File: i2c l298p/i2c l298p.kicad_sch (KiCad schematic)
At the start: 119 parts, among them J1 power in, J2 Conn_01x04, J4 Conn_01x04, J6 to qwiic breakout, J7 qwiic 1, J8 qwiic 2, U1 ILQ620GB-X009, U2 ILQ620GB-X009, U3 ILQ620GB-X009, U5 PCA9685PW

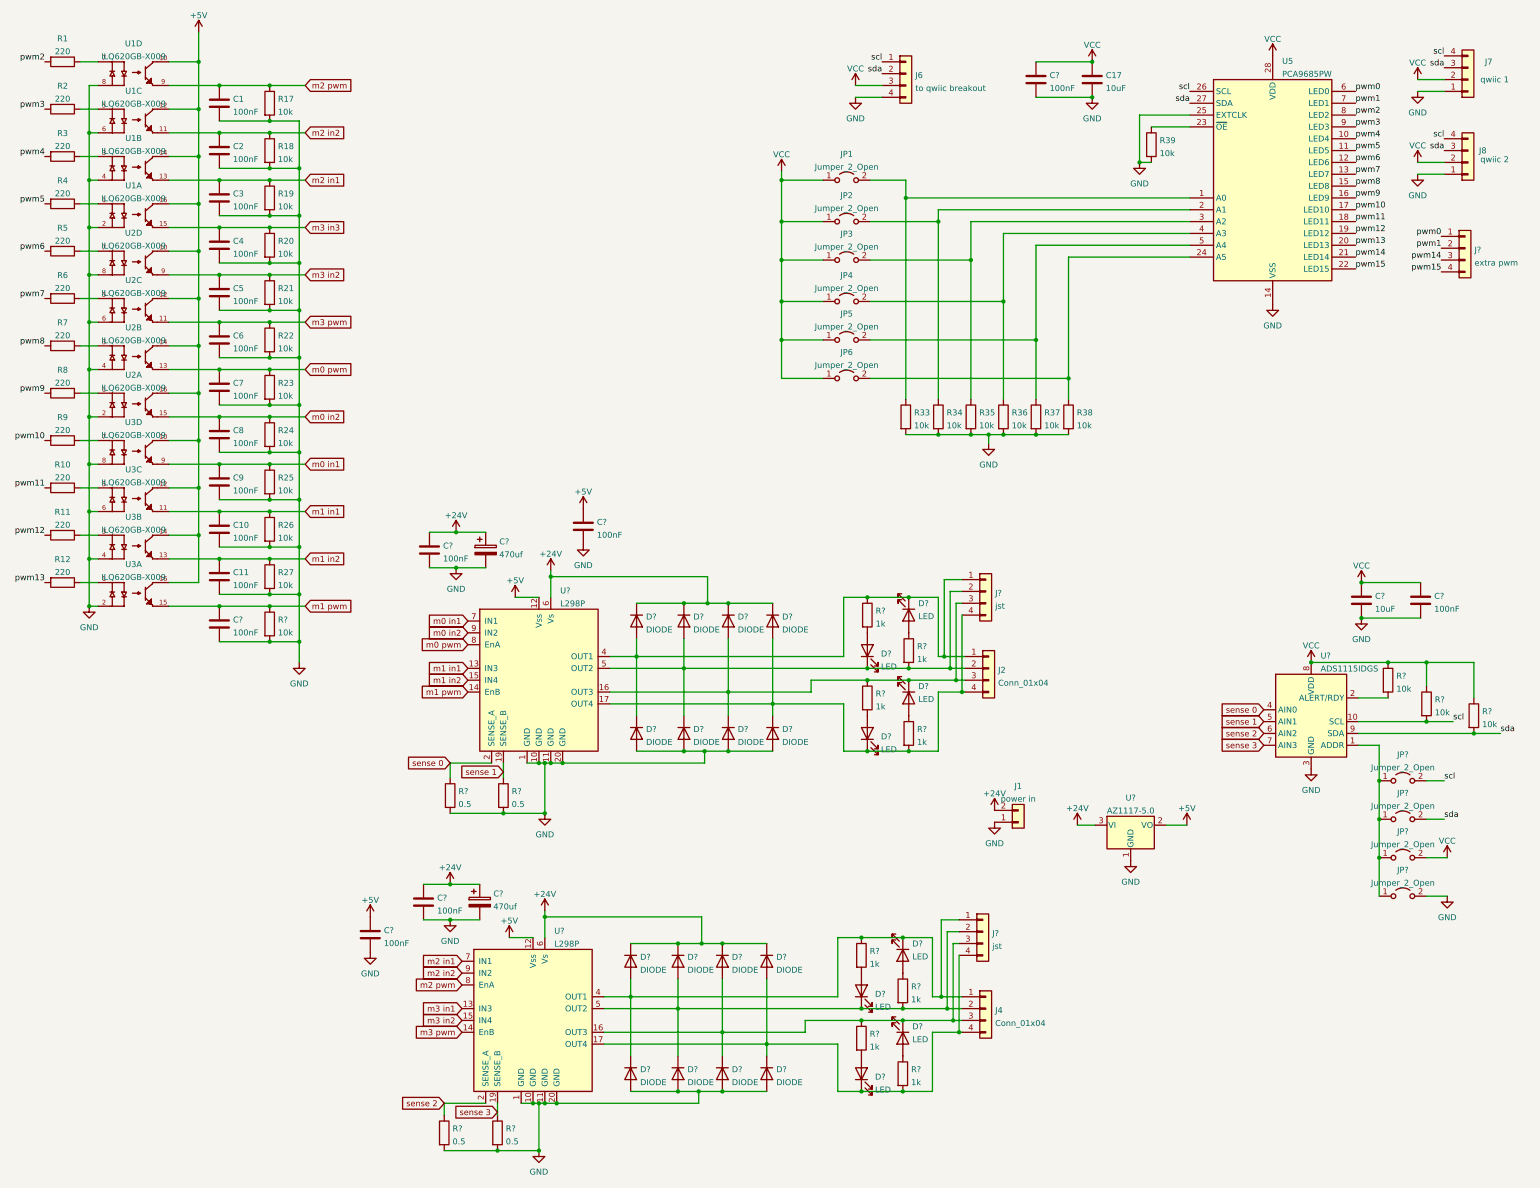
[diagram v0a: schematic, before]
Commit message: finished motor controller layout
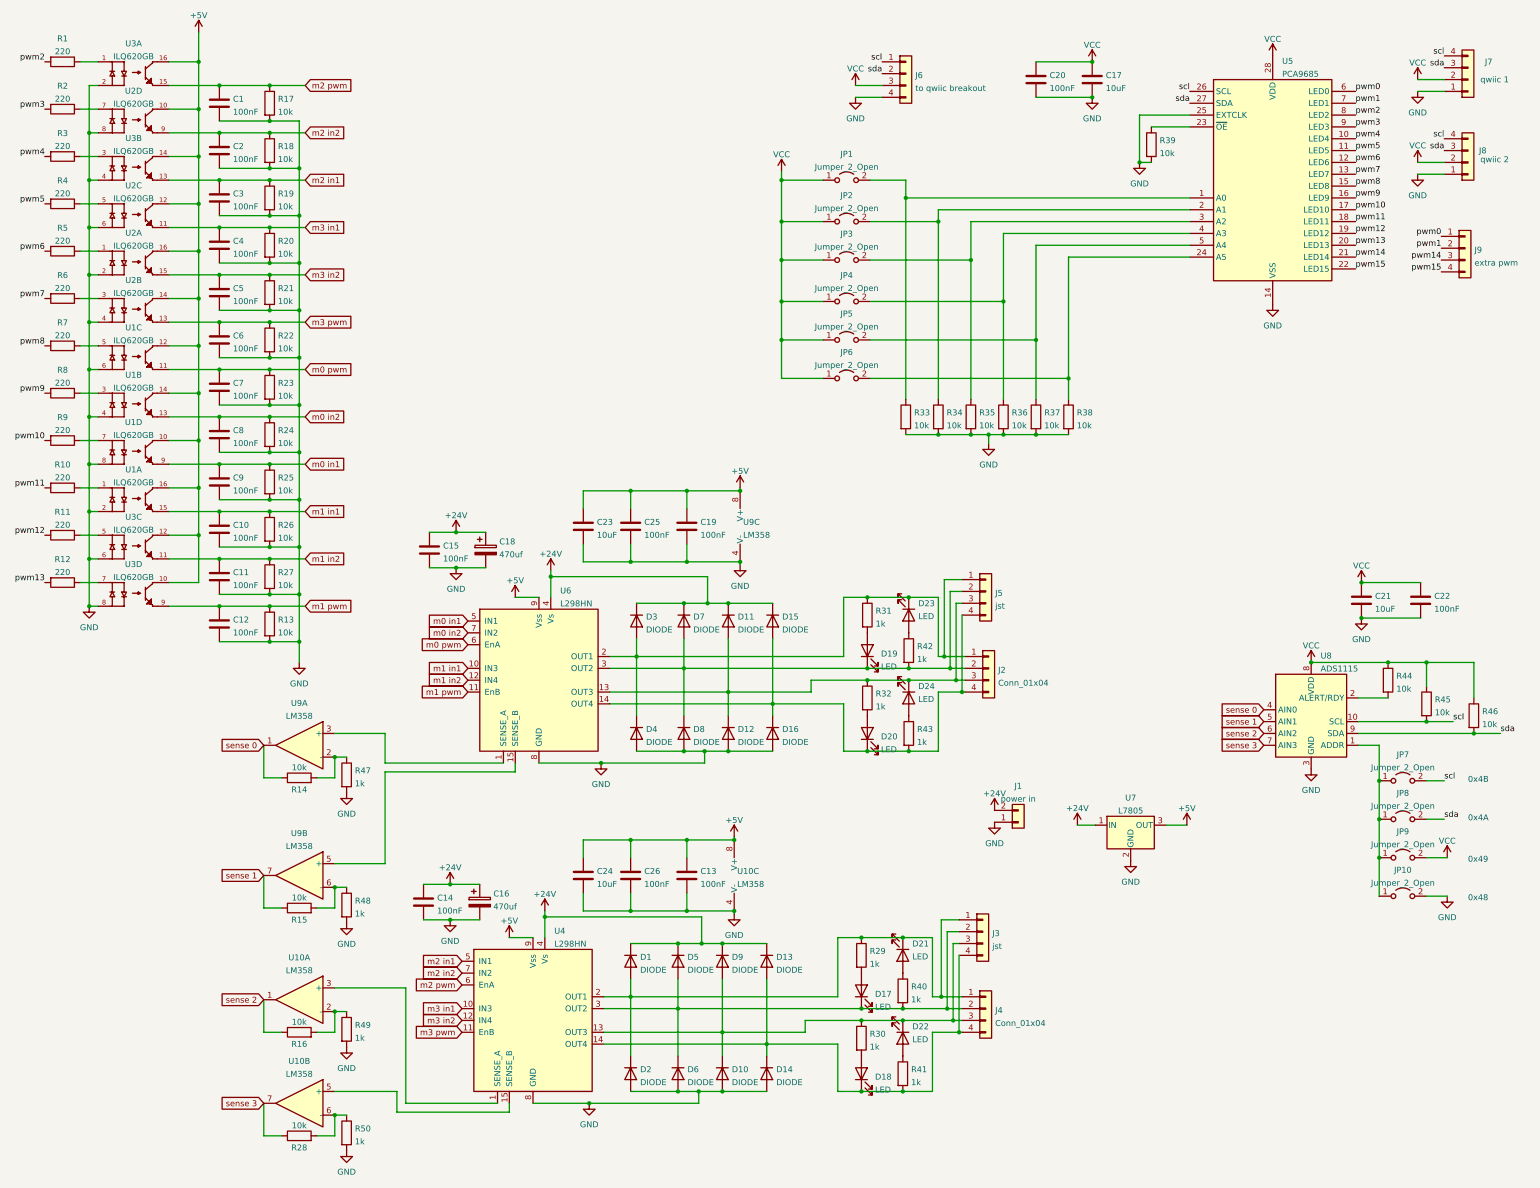
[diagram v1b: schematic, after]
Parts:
- removed R? (x4): 0.5, symbol Device:R
- removed U? (x2): L298P, symbol Driver_Motor:L298P
- removed U?: AZ1117-5.0, symbol Regulator_Linear:AZ1117-5.0
- added C23, C24: 10uF, Capacitor_SMD:C_0603_1608Metric, symbol Device:C
- added C25, C26: 100nF, Capacitor_SMD:C_0603_1608Metric, symbol Device:C
- added R14, R15, R16, R28: 10k, Resistor_SMD:R_0603_1608Metric, symbol Device:R
- added R47, R48, R49, R50: 1k, Resistor_SMD:R_0603_1608Metric, symbol Device:R
- added U10, U9: LM358, Package_SO:SOIC-8_3.9x4.9mm_P1.27mm, symbol Amplifier_Operational:LM358
- added U4, U6: L298HN, Package_TO_SOT_THT:TO-220-15_P2.54x2.54mm_StaggerOdd_Lead4.58mm_Vertical, symbol Driver_Motor:L298HN
- added U7: L7805, Package_TO_SOT_THT:TO-220-3_Horizontal_TabDown, symbol Regulator_Linear:L7805
- C16, C18: renamed from C?; footprint (none) -> Capacitor_THT:CP_Radial_D8.0mm_P3.50mm
- D1, D10, D11, D12, D13, D14, D15, D16, D2, D3, D4, D5, D6, D7, D8, D9: renamed from D?; footprint (none) -> Diode_SMD:D_SMA
- D17, D18, D19, D20, D21, D22, D23, D24: renamed from D?; footprint (none) -> LED_SMD:LED_0603_1608Metric
- J3, J5: renamed from J?; footprint TerminalBlock_Phoenix:TerminalBlock_Phoenix_MKDS-1,5-4_1x04_P5.00mm_Horizontal -> Connector_JST:JST_XH_B4B-XH-A_1x04_P2.50mm_Vertical
- J9: renamed from J?; footprint (none) -> Connector_PinHeader_2.54mm:PinHeader_1x04_P2.54mm_Vertical
- R29, R30, R31, R32, R40, R41, R42, R43: renamed from R?; footprint (none) -> Resistor_SMD:R_0603_1608Metric
- U1, U2, U3: value ILQ620GB-X009 -> ILQ620GB
- U5: value PCA9685PW -> PCA9685
- U8: renamed from U?; value ADS1115IDGS -> ADS1115
- gave numbers to parts that had none: 16
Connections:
- net +24V: now also U4.4 (Vs), U6.4 (Vs), U7.1 (IN)
- net +5V: now also C23.1, C24.1, C25.1, C26.1, U10.8 (V+), U4.9 (Vss), U6.9 (Vss), U7.3 (OUT), U9.8 (V+)
- net GND: now also C23.2, C24.2, C25.2, C26.2, R47.2, R48.2, R49.2, R50.2, U10.4 (V-), U4.8 (GND), U6.8 (GND), U7.2 (GND), U9.4 (V-)
- net m0 in1: now also U1.9, U6.5 (IN1); no longer U3.9
- net m0 in2: now also U1.13, U6.7 (IN2); no longer U2.15
- net m0 pwm: now also U1.11, U6.6 (EnA); no longer U2.13
- net m1 in1: now also U1.15, U6.10 (IN3); no longer U3.11
- net m1 in2: now also U3.11, U6.12 (IN4); no longer U3.13
- net m1 pwm: now also U3.9, U6.11 (EnB); no longer U3.15
- net m2 in1: now also U3.13, U4.5 (IN1); no longer U1.13
- net m2 in2: now also U2.9, U4.7 (IN2); no longer U1.11
- net m2 pwm: now also U3.15, U4.6 (EnA); no longer U1.9
- net m3 in1: now also C4.1, R20.1, U2.11, U4.10 (IN3)
- net m3 in2: now also U2.15, U4.12 (IN4); no longer U2.9
- net m3 pwm: now also U2.13, U4.11 (EnB); no longer U2.11
- net sense 0: now also R14.1, U9.1
- net sense 1: now also R15.1, U9.7
- net sense 2: now also R16.1, U10.1
- net sense 3: now also R28.1, U10.7
- net at D23.1 (K), D3.1 (A), D4.2 (K)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: now also U6.2 (OUT1)
- net at R6.1: now also U2.3; no longer U2.5
- net at D17.1 (K), D5.1 (A), D6.2 (K)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: now also U4.3 (OUT2)
- net at U1.3: now also R8.1; no longer R3.1
- net at U2.1: now also R5.1; no longer R8.1
- net at D15.1 (A), D16.2 (K), D20.1 (K)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: now also U6.14 (OUT4)
- net at R7.1: now also U1.5; no longer U2.3
- net at R12.1: now also U3.7; no longer U3.1
- net at D10.2 (K), D22.1 (K), D9.1 (A)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: now also U4.13 (OUT3)
- net at R1.1: now also U3.1; no longer U1.7
- net at R9.1: now also U1.7; no longer U3.7
- net at D13.1 (A), D14.2 (K), D18.1 (K)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: now also U4.14 (OUT4)
- net at D1.1 (A), D2.2 (K), D21.1 (K)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: now also U4.2 (OUT1)
- net at U2.7: now also R2.1; no longer R5.1
- net at R11.1: now also U3.5; no longer U3.3
- net at D11.1 (A), D12.2 (K), D24.1 (K)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: now also U6.13 (OUT3)
- net at D19.1 (K), D7.1 (A), D8.2 (K)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: now also U6.3 (OUT2)
- net at R4.1: now also U2.5; no longer U1.1
- net at R10.1: now also U1.1; no longer U3.5
- removed net m3 in3: C4.1, R20.1, U1.15
- new net: R15.2, R48.1, U9.6 (-)
- new net: R14.2, R47.1, U9.2 (-)
- new net: U6.1 (SENSE_A), U9.3 (+)
- new net: R28.2, R50.1, U10.6 (-)
- new net: U6.15 (SENSE_B), U9.5 (+)
- new net: U10.3 (+), U4.1 (SENSE_A)
- new net: U10.5 (+), U4.15 (SENSE_B)
- new net: R16.2, R49.1, U10.2 (-)
- new net: R3.1, U3.3
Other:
- note added: "0x48"
- note added: "0x49"
- note added: "0x4A"
- note added: "0x4B"
- moved on the sheet: C13, C19
